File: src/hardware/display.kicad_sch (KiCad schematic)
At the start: 7 parts

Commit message: Renamed symboles, added 3D models
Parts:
- removed J?: 046809612110846+, 046809612110846, symbol 046809612110846+:046809612110846+
- removed U?: TXS0108EQWRKSRQ1, RKS0020B-MFG, symbol 2026-10-21_15-51-24:TXS0108EQWRKSRQ1
- removed U?: LP5817YCHR, DSBGA-8_YCH0008_TEX, symbol 2026-10-21_16-01-06:LP5817YCHR
- added J?: 046809612110846+, 046809612110846, symbol 046809612110846+:046809612110846+
- added U?: LP5817YCHR, DSBGA-8_YCH0008_TEX, symbol LP5817YCHR:LP5817YCHR
- added U?: TXS0108EQWRKSRQ1, RKS0020B-MFG, symbol TXS0108EQWRKSRQ1:TXS0108EQWRKSRQ1
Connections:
- net +1V8: now also J?.8, U?.2 (VCCA)
- net +3V0: now also J?.12
- net +3V3: now also U?.19 (VCCB), U?.D1 (VCC)
- net CS: now also J?.2, U?.1 (A1)
- net DC: now also J?.3, U?.3 (A2)
- net GND: now also J?.1, J?.13, J?.14, J?.9, U?.11 (GND), U?.21 (Thermal_Pad), U?.C1 (GND), U?.D2 (NC)
- net LCDCMD: now also U?.18 (B2)
- net LCDCS: now also U?.20 (B1)
- net LCDTE: now also U?.14 (B6)
- net LCD\RESET: now also U?.17 (B3)
- net LEDK: now also J?.10, J?.11, U?.A2 (OUT0)
- net MOSI: now also U?.15 (B5)
- net RST: now also J?.4, U?.4 (A3)
- net SCK: now also U?.16 (B4)
- net SCL: now also J?.5, U?.5 (A4), U?.A1 (SCL)
- net SDA: now also J?.6, U?.6 (A5), U?.B1 (SDA)
- net TE: now also J?.7, U?.7 (A6)
- net at R?.1: now also U?.10 (OE)
- net at D?.1 (K1): now also U?.B2 (OUT1)
- net at D?.2 (K2): now also U?.C2 (OUT2)

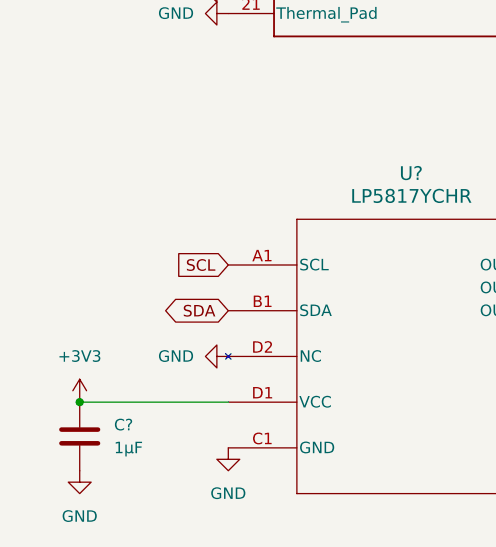
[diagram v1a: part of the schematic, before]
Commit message: Added missing I²C Address
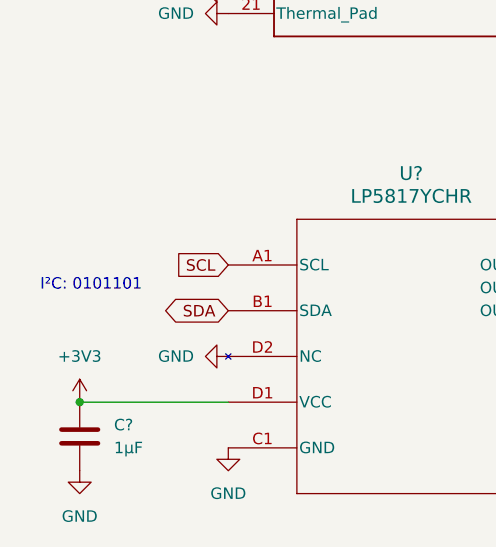
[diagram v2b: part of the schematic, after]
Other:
- note added: "I²C: 0101101"
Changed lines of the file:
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@@
 		(date "2026-10-21")
+	)
+	(text "I²C: 0101101"
+		(exclude_from_sim no)
+		(at 91.44 128.016 0)
+		(effects
+			(font
+				(size 1.27 1.27)
+			)
+		)
 	)
 	(junction

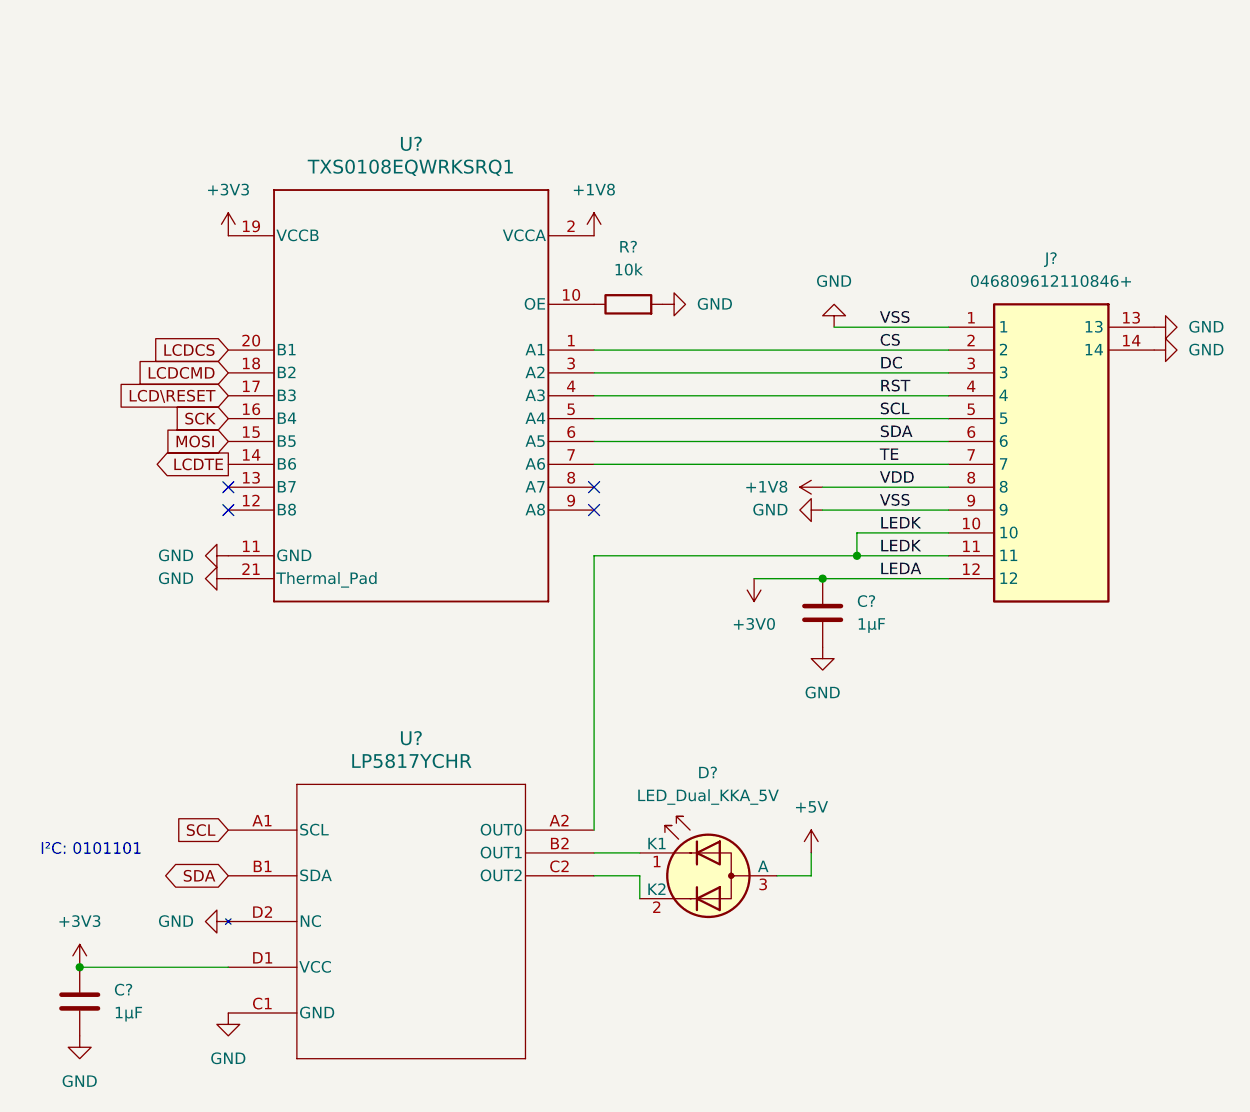
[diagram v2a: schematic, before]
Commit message: Replaced schematics, 3d models and footprints. Added vibration motor.
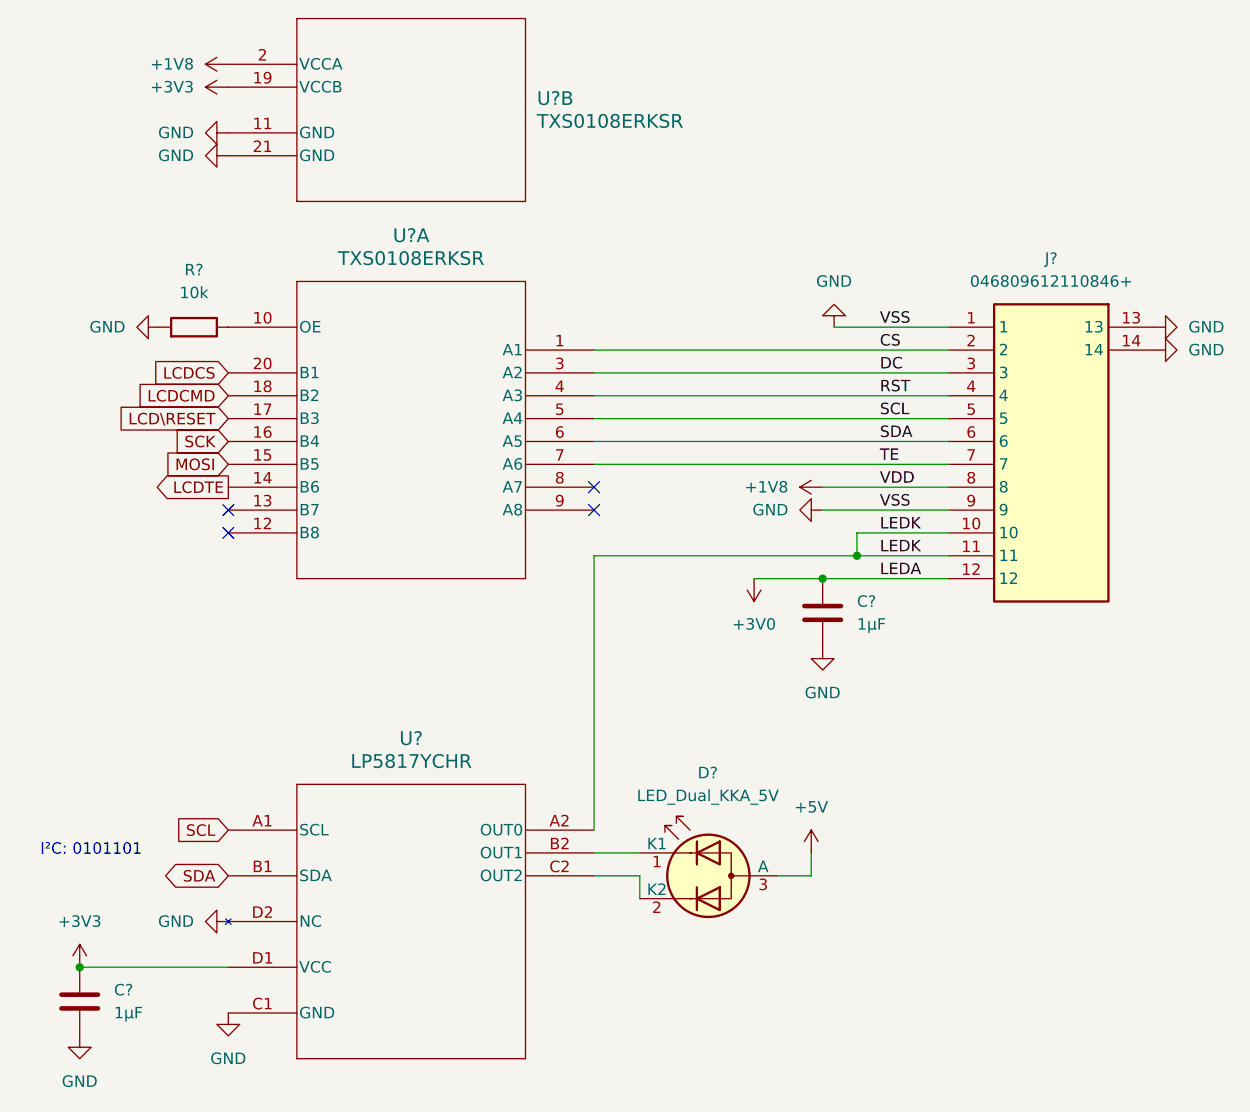
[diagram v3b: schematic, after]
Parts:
- removed J?: 046809612110846+, 046809612110846, symbol 046809612110846+:046809612110846+
- removed U?: LP5817YCHR, DSBGA-8_YCH0008_TEX, symbol LP5817YCHR:LP5817YCHR
- removed U?: TXS0108EQWRKSRQ1, RKS0020B-MFG, symbol TXS0108EQWRKSRQ1:TXS0108EQWRKSRQ1
- added J?: 046809612110846+, 046809612110846, symbol 046809612110846+:046809612110846+
- added U? (x2): TXS0108ERKSR, VQFN20_RKS_TEX, symbol TXS0108ERKSR:TXS0108ERKSR
- added U?: LP5817YCHR, DSBGA-8_YCH0008_TEX, symbol LP5817YCHR:LP5817YCHR
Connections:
- net +1V8: now also J?.8, U?.2 (VCCA)
- net +3V0: now also J?.12
- net +3V3: now also U?.19 (VCCB), U?.D1 (VCC)
- net CS: now also J?.2, U?.1 (A1)
- net DC: now also J?.3, U?.3 (A2)
- net GND: now also J?.1, J?.13, J?.14, J?.9, U?.11 (GND), U?.21 (GND), U?.C1 (GND), U?.D2 (NC)
- net LCDCMD: now also U?.18 (B2)
- net LCDCS: now also U?.20 (B1)
- net LCDTE: now also U?.14 (B6)
- net LCD\RESET: now also U?.17 (B3)
- net LEDK: now also J?.10, J?.11, U?.A2 (OUT0)
- net MOSI: now also U?.15 (B5)
- net RST: now also J?.4, U?.4 (A3)
- net SCK: now also U?.16 (B4)
- net SCL: now also J?.5, U?.5 (A4), U?.A1 (SCL)
- net SDA: now also J?.6, U?.6 (A5), U?.B1 (SDA)
- net TE: now also J?.7, U?.7 (A6)
- net at R?.1: now also U?.10 (OE)
- net at D?.1 (K1): now also U?.B2 (OUT1)
- net at D?.2 (K2): now also U?.C2 (OUT2)
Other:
- moved on the sheet: R?

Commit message: Added LoRa
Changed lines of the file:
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@@
 		)
 		(property "Value" "GND"
-			(at 106.68 151.13 0)
-			(effects
-				(font
-					(size 1.27 1.27)
-				)
+			(at 104.14 147.3199 0)
+			(effects
+				(font
+					(size 1.27 1.27)
+				)
+				(justify right)
 			)
 		)
@@
 		(on_board yes)
 		(dnp no)
+		(fields_autoplaced yes)
 		(property "Reference" "J?"
 			(at 198.12 62.23 0)

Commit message: Selected GPIO
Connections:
- net HRINT: now reaches U?.13 (B7)
- net HRINT1V8: now reaches U?.8 (A7)
- no-connect marks 4 -> 2
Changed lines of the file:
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@@
-	)
-	(no_connect
-		(at 147.32 87.63)
 	)
 	(no_connect
 		(at 106.68 92.71)
 	)
-	(no_connect
-		(at 106.68 90.17)
-	)
 	(wire
 		(pts
@@
 	(wire
 		(pts
+			(xy 147.32 95.25) (xy 176.53 95.25)
+		)
+		(stroke
+			(width 0)
+			(type default)
+		)
+	)
+	(wire
+		(pts
+			(xy 152.4 130.81) (xy 152.4 133.35)
+		)
+		(stroke
+			(width 0)
+			(type default)
+		)
+	)
+	(wire
+		(pts
+			(xy 171.45 128.27) (xy 171.45 130.81)
+		)
+		(stroke
+			(width 0)
+			(type default)
+		)
+	)
+	(wire
+		(pts
+			(xy 176.53 92.71) (xy 186.69 92.71)
+		)
+		(stroke
+			(width 0)
+			(type default)
+		)
+	)
+	(wire
+		(pts
 			(xy 147.32 85.09) (xy 186.69 85.09)
-		)
-		(stroke
-			(width 0)
-			(type default)
-		)
-	)
-	(wire
-		(pts
-			(xy 147.32 95.25) (xy 176.53 95.25)
-		)
-		(stroke
-			(width 0)
-			(type default)
-		)
-	)
-	(wire
-		(pts
-			(xy 152.4 130.81) (xy 152.4 133.35)
-		)
-		(stroke
-			(width 0)
-			(type default)
-		)
-	)
-	(wire
-		(pts
-			(xy 171.45 128.27) (xy 171.45 130.81)
-		)
-		(stroke
-			(width 0)
-			(type default)
-		)
-	)
-	(wire
-		(pts
-			(xy 176.53 92.71) (xy 186.69 92.71)
 		)
 		(stroke
@@
 		)
 	)
+	(global_label "HRINT"
+		(shape output)
+		(at 106.68 90.17 180)
+		(fields_autoplaced yes)
+		(effects
+			(font
+				(size 1.27 1.27)
+			)
+			(justify right)
+		)
+		(property "Intersheetrefs" "${INTERSHEET_REFS}"
+			(at 98.1914 90.17 0)
+			(effects
+				(font
+					(size 1.27 1.27)
+				)
+				(justify right)
+				(hide yes)
+			)
+		)
+	)
 	(global_label "LCDTE"
 		(shape output)
@@
 				)
 				(justify right)
+				(hide yes)
+			)
+		)
+	)
+	(global_label "HRINT1V8"
+		(shape input)
+		(at 147.32 87.63 0)
+		(fields_autoplaced yes)
+		(effects
+			(font
+				(size 1.27 1.27)
+			)
+			(justify left)
+		)
+		(property "Intersheetrefs" "${INTERSHEET_REFS}"
+			(at 159.3162 87.63 0)
+			(effects
+				(font
+					(size 1.27 1.27)
+				)
+				(justify left)
 				(hide yes)
 			)
@@
 		)
 		(property "Value" "+5V"
-			(at 171.45 123.19 0)
-			(effects
-				(font
-					(size 1.27 1.27)
-				)
+			(at 173.99 126.9999 0)
+			(effects
+				(font
+					(size 1.27 1.27)
+				)
+				(justify left)
 			)
 		)
@@
 		)
 		(property "Value" "+3V0"
-			(at 165.1 102.87 0)
-			(effects
-				(font
-					(size 1.27 1.27)
-				)
+			(at 162.56 99.0599 0)
+			(effects
+				(font
+					(size 1.27 1.27)
+				)
+				(justify left)
 			)
 		)
@@
 		)
 		(property "Value" "GND"
-			(at 95.25 69.8499 90)
-			(effects
-				(font
-					(size 1.27 1.27)
-				)
-				(justify right)
-			)
-		)
+			(at 97.79 66.04 90)
+			(effects
+				(font
+					(size 1.27 1.27)
+				)
+			)
+		)

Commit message: Changed 5V net to 4.5V net
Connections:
- net +5V renamed +4V5
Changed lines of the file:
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@@
 			)
 		)
-		(property "Value" "+5V"
+		(property "Value" "+4V5"
 			(at 173.99 126.9999 0)
 			(effects

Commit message: Added Accelerometer Clock; Cleanup & Fixes
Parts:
- R?: value 10k -> 10kΩ
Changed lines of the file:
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@@
 			)
 		)
-		(property "Value" "10k"
+		(property "Value" "10kΩ"
 			(at 102.87 66.04 90)
 			(effects

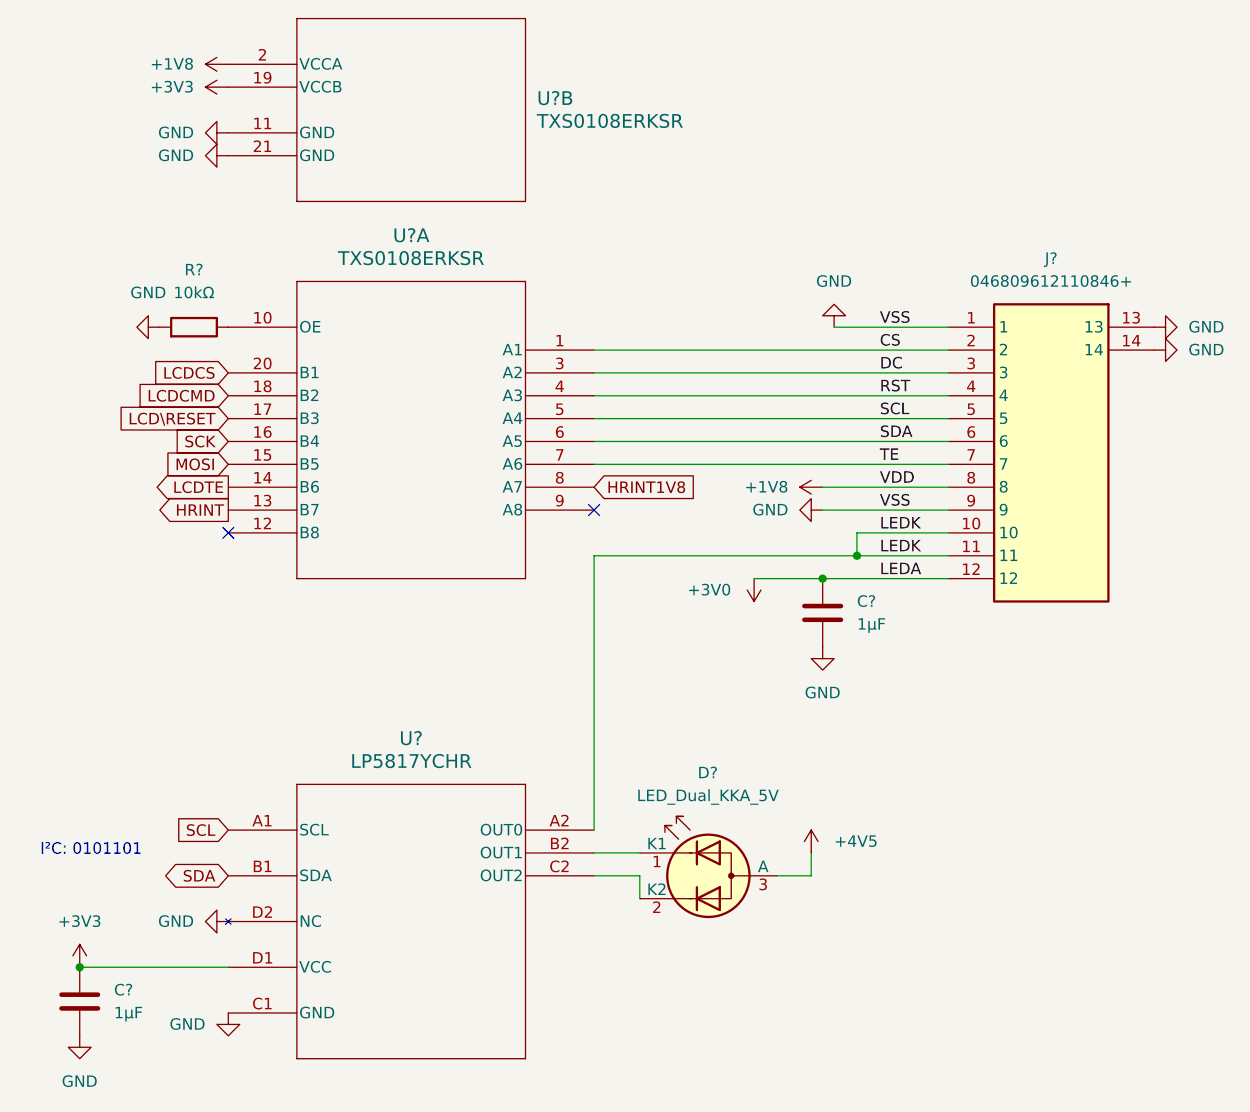
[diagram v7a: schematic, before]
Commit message: Cleanup & Fixes; Added footprints; Removed Light sensors
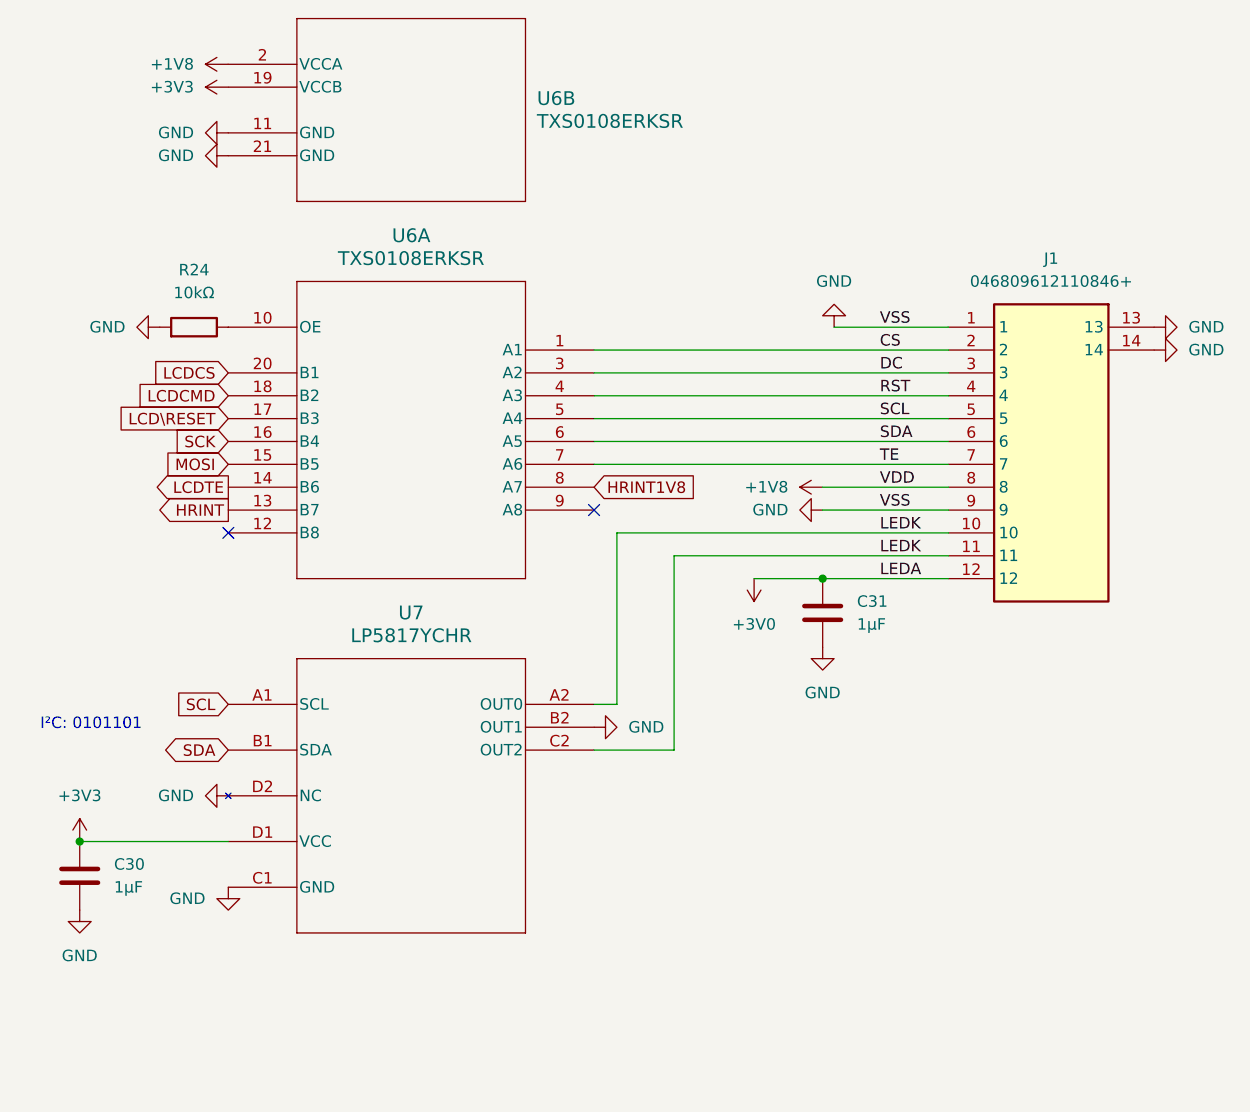
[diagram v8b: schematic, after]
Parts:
- removed D?: LED_Dual_KKA_5V, symbol Device:LED_Dual_KKA
- C30, C31: renamed from C?; footprint (none) -> Capacitor_SMD:C_0603_1608Metric
- J1: renamed from J?; footprint 046809612110846 -> Project:046809612110846
- R24: renamed from R?; footprint (none) -> Resistor_SMD:R_0603_1608Metric
- U6: renamed from U?; footprint VQFN20_RKS_TEX -> Project:VQFN20_RKS_TEX
- U7: renamed from U?; footprint DSBGA-8_YCH0008_TEX -> Project:DSBGA-8_YCH0008_TEX
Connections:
- net GND: now also U7.B2 (OUT1)
- net LEDK: now also U7.C2 (OUT2)
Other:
- moved on the sheet: C30, U7
